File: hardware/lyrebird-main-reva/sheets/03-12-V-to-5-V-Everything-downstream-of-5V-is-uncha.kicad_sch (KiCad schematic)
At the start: 11 parts, among them U5 LMR33630 12V->5V 3A

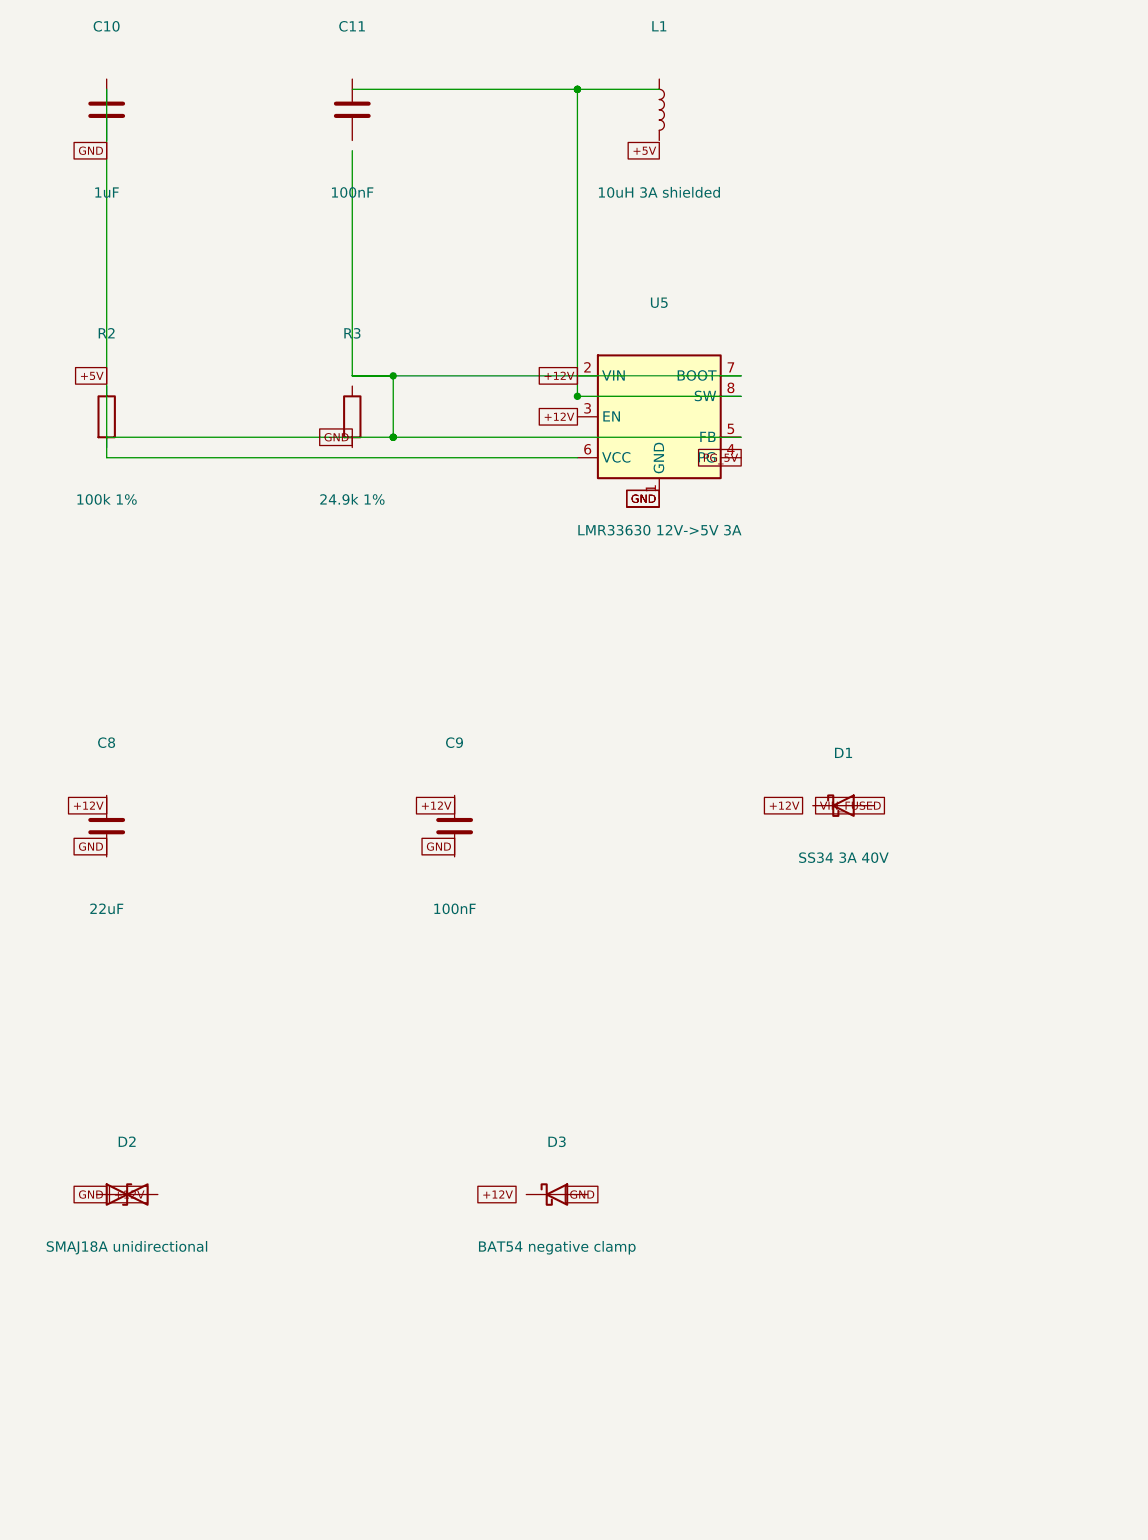
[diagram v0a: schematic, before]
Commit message: Connect two power-good nets that were connected to nothing
The schematic validator found a confirmed fault, and it is the kind that
reads as correct code. `Net("PG_5V")` appears twice in main_board.py --
once to attach the buck's power-good pin, once to attach its pull-up --
and SKiDL creates a NEW net on each call, uniquifying the second name.
The result was four single-node nets: both LMR33630 power-good pins
alone, and both 100 k resistors with one lead floating.

The inverter's half mattered more than the buck's. U7's GND pin *is*
-6V_A, so 100 k to system ground is a pull-up relative to the device and
the only way that flag can be read at all. It was reading nothing.

Both now use one Net object and reuse it, which is what every other net
in both generators already did -- the defect was exactly two instances of
one idiom, not a pattern. I checked: MCLK is also written as
Net("MCLK") twice, but once per file on different boards, so it is
whole in each netlist.

The more useful outcome is a check. A net with one node connects
nothing, and nothing in the generation path said so -- KiCad ERC would
have, on import, and nothing runs ERC. check_freshness.py now reports
single-node nets on both boards, with the module's four reserved element
lines exempted because interface.md requires the main board to drive
them and they are correctly bare on the module side. Tamper-tested by
reintroducing the idiom: it names PG_5V and PG_5V1 and fails.

Co-Authored-By: Claude Opus 5 <noreply@anthropic.com>
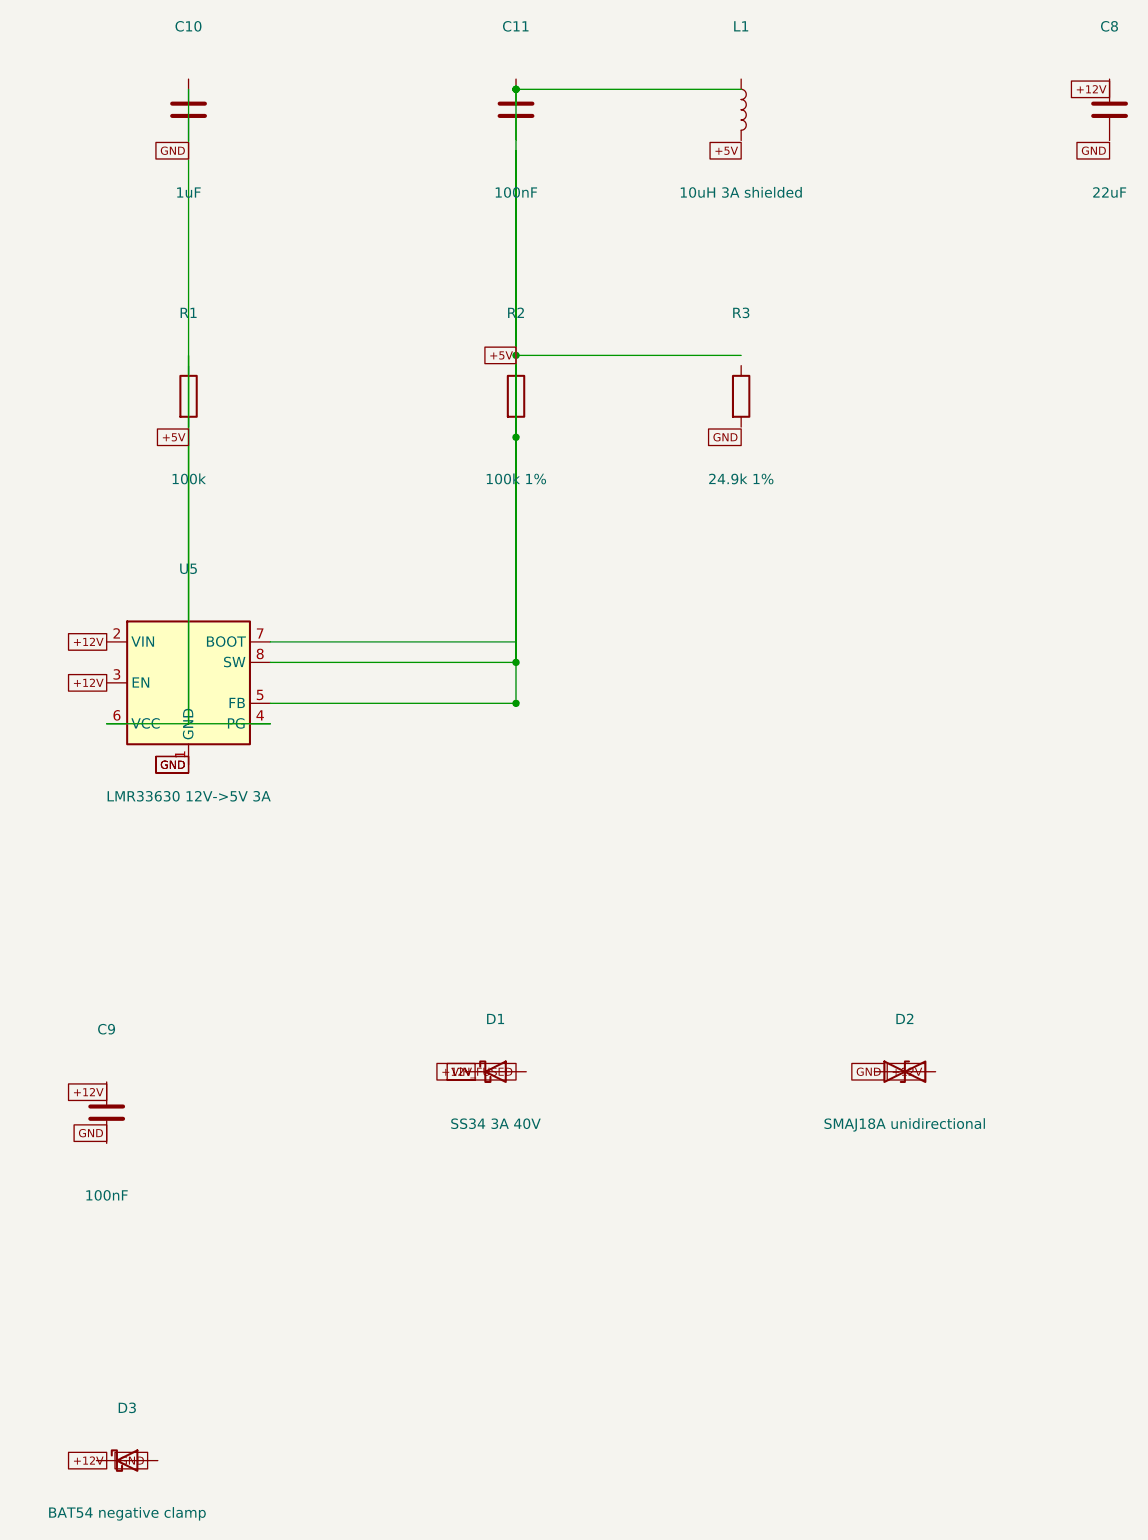
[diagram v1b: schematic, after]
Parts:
- added D3: BAT54 negative clamp, symbol Device:D_Schottky
- C8: renamed from C9; value 100nF -> 22uF
- C9: renamed from D1; value SS34 3A 40V -> 100nF; symbol Device:D_Schottky -> Device:C
- D1: renamed from D2; value SMAJ18A unidirectional -> SS34 3A 40V; symbol Device:D_TVS -> Device:D_Schottky
- D2: renamed from D3; value BAT54 negative clamp -> SMAJ18A unidirectional; symbol Device:D_Schottky -> Device:D_TVS
- R1: renamed from R2; value 100k 1% -> 100k
- R2: renamed from R3; value 24.9k 1% -> 100k 1%
- R3: renamed from U5; value LMR33630 12V->5V 3A -> 24.9k 1%; symbol Regulator_Switching:LMR33630ADDA -> Device:R
- U5: renamed from C8; value 22uF -> LMR33630 12V->5V 3A; symbol Device:C -> Regulator_Switching:LMR33630ADDA
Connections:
- net +12V: now also U5.2 (VIN), U5.3 (EN); no longer R3.1 (GND), R3.2 (VIN), R3.3 (EN), R3.5 (FB), R3.6 (VCC), R3.7 (BOOT), R3.8 (SW), R3.9 (GND)
- net +5V: now reaches U5.1 (GND)
- net +5V: now also U5.4 (PG), U5.5 (FB), U5.6 (VCC), U5.7 (BOOT), U5.8 (SW), U5.9 (GND)
- removed net PG_5V: R3.4 (PG)
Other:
- moved on the sheet: C10, C11, C8, D1, D2, L1, R1, R2

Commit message: Act on the schematic validation: three faults and the core-rail guard
**The SuperSpeed pairs were wired backwards, and are now not wired.**
USB_SSRX_P/N were the only multi-node nets on the board with an INPUT at
every pin -- the receptacle's SSRX pins are inputs and so are the
bridge's RIDP/RIDN, so nothing drove them, and the transmit pair was
mirrored the same way. The comment asserted a crossover inside the cable
as fact and reasoned from it; USB 3.0 cables have no crossover.
SuperSpeed would never have trained and the link would have fallen back
to 480 Mb/s silently -- which is the speed 0014 chose on purpose, since
no galvanic isolator exists above USB 2.0. So the pairs are removed
rather than corrected, which also retires the hardest constraint in this
board's layout. How to wire them correctly if they ever come back is
recorded where they were.

**The inverting converter had no input capacitor across its own
terminals.** Nothing spanned +12V and -6V_A, and U7's GND pin *is*
-6V_A, so the loop its switching current actually takes was unbypassed
-- the input caps near U5 are referenced to system ground and are not in
that loop at all. This is the third fault found in U7 and all three are
the same mistake: reasoning about it as though its ground were the
board's.

**The translator's output enables are tied low against an explicit
datasheet instruction**, and the fix is sequencing rather than a pull-up.
SCES576I says OE must be pulled up to VCCA and not enabled until both
supplies are stable; a pull-up is not available here because nothing on
the module could pull it down -- no spare mezzanine pin, and MUTE_N has
the wrong polarity. Instead VCC(A) is made the last rail to arrive:
10 uF on U9's SET gives 573 ms against 359 ms for VCC(B), so the enable
cannot precede the supply it switches to. It costs nothing, because that
rail feeds the translator's reference supply and nothing else.

**The core rail now has a guard, and it needed two attempts.** The
existing as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
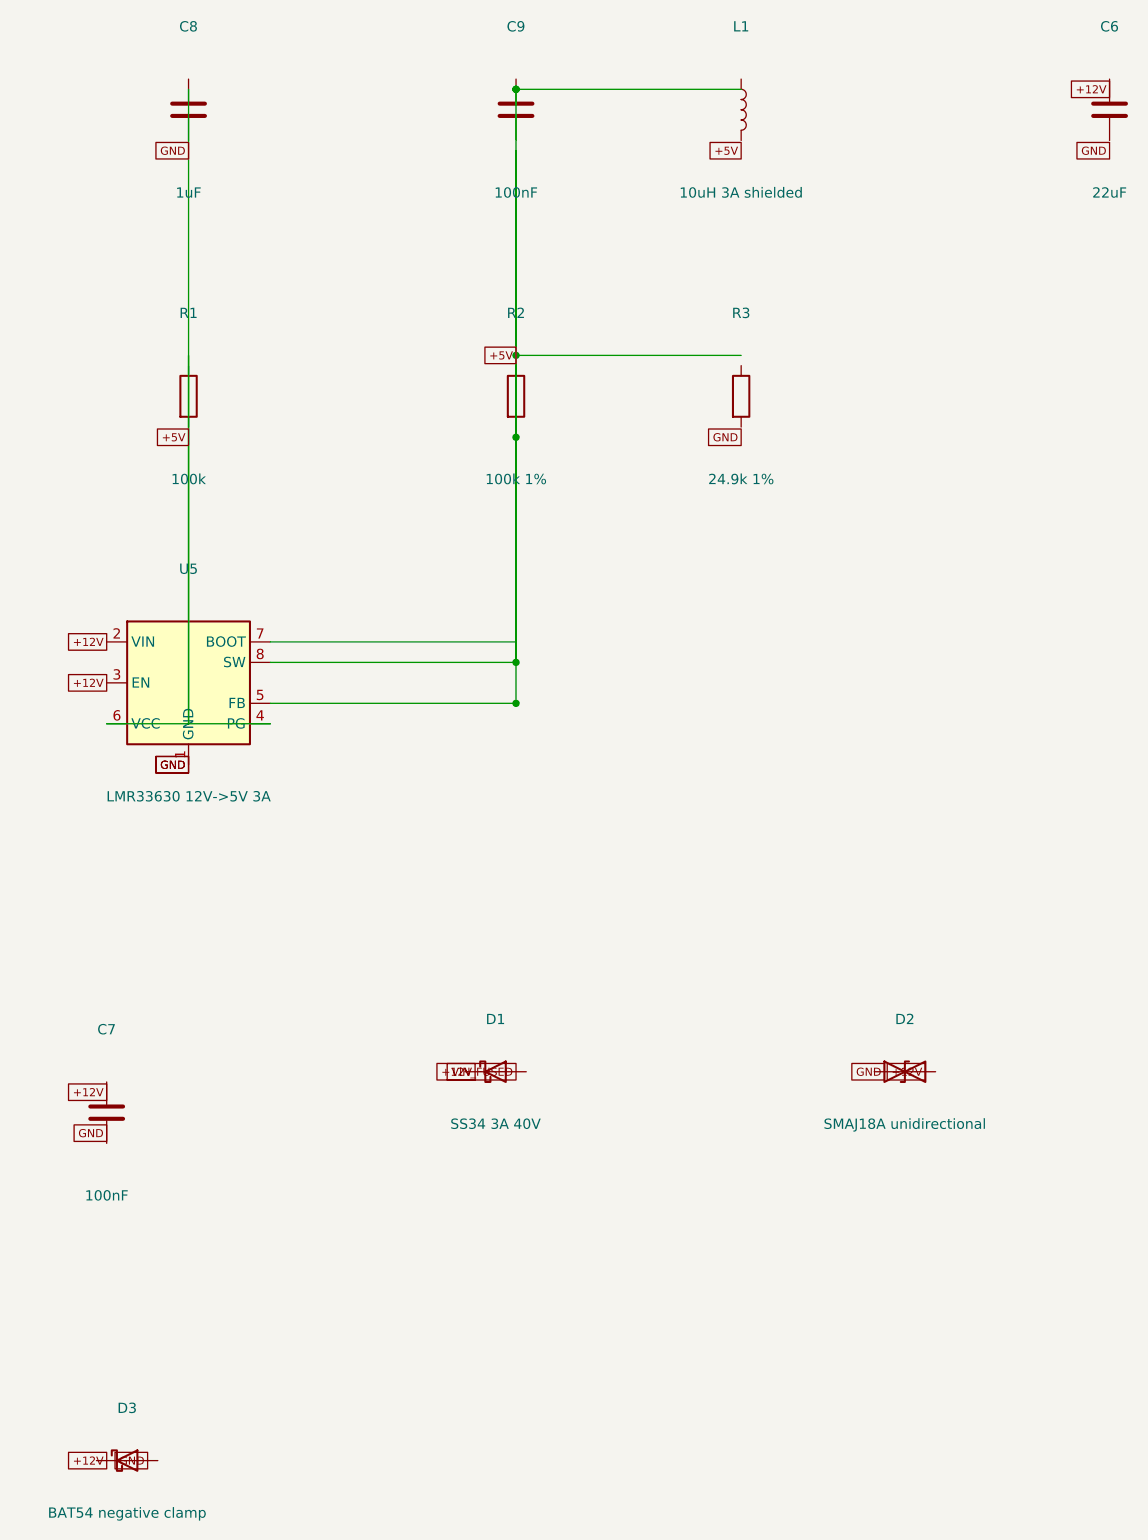
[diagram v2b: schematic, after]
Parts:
- renumbered C8 to C6, C9 to C7, C10 to C8, C11 to C9
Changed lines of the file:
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@@
 	(symbol (lib_id "Device:C") (at 45.72 35.56 0) (unit 1)
 		(exclude_from_sim no) (in_bom yes) (on_board yes) (dnp no)
-		(property "Reference" "C10" (at 45.72 25.250000000000004 0)
+		(property "Reference" "C8" (at 45.72 25.250000000000004 0)
 			(effects (font (size 1.27 1.27))))
 		(property "Value" "1uF" (at 45.72 45.870000000000005 0)
 			(effects (font (size 1.27 1.27))))
-		(instances (project "" (path "/" (reference "C10") (unit 1))))
+		(instances (project "" (path "/" (reference "C8") (unit 1))))
 	)
 	(symbol (lib_id "Device:C") (at 86.36 35.56 0) (unit 1)
 		(exclude_from_sim no) (in_bom yes) (on_board yes) (dnp no)
-		(property "Reference" "C11" (at 86.36 25.250000000000004 0)
+		(property "Reference" "C9" (at 86.36 25.250000000000004 0)
 			(effects (font (size 1.27 1.27))))
 		(property "Value" "100nF" (at 86.36 45.870000000000005 0)
 			(effects (font (size 1.27 1.27))))
-		(instances (project "" (path "/" (reference "C11") (unit 1))))
+		(instances (project "" (path "/" (reference "C9") (unit 1))))
 	)
 	(symbol (lib_id "Device:L") (at 114.3 35.56 0) (unit 1)
@@
 	(symbol (lib_id "Device:C") (at 160.02 35.56 0) (unit 1)
 		(exclude_from_sim no) (in_bom yes) (on_board yes) (dnp no)
-		(property "Reference" "C8" (at 160.02 25.250000000000004 0)
+		(property "Reference" "C6" (at 160.02 25.250000000000004 0)
 			(effects (font (size 1.27 1.27))))
 		(property "Value" "22uF" (at 160.02 45.870000000000005 0)
 			(effects (font (size 1.27 1.27))))
-		(instances (project "" (path "/" (reference "C8") (unit 1))))
+		(instances (project "" (path "/" (reference "C6") (unit 1))))
 	)
 	(symbol (lib_id "Device:C") (at 35.56 160.02 0) (unit 1)
 		(exclude_from_sim no) (in_bom yes) (on_board yes) (dnp no)
-		(property "Reference" "C9" (at 35.56 149.71 0)
+		(property "Reference" "C7" (at 35.56 149.71 0)
 			(effects (font (size 1.27 1.27))))
 		(property "Value" "100nF" (at 35.56 170.33 0)
 			(effects (font (size 1.27 1.27))))
-		(instances (project "" (path "/" (reference "C9") (unit 1))))
+		(instances (project "" (path "/" (reference "C7") (unit 1))))
 	)
 	(symbol (lib_id "Device:D_Schottky") (at 83.82000000000001 154.94 0) (unit 1)
@@
 		(effects (font (size 1.0 1.0)) (justify right))
 )
-	(global_label "GND" (shape passive) (at 45.72 40.64 0)
-		(effects (font (size 1.0 1.0)) (justify right))
-)
 	(global_label "GND" (shape passive) (at 160.02 40.64 0)
 		(effects (font (size 1.0 1.0)) (justify right))
@@
 		(effects (font (size 1.0 1.0)) (justify right))
 )
+	(global_label "GND" (shape passive) (at 45.72 40.64 0)
+		(effects (font (size 1.0 1.0)) (justify right))
+)
